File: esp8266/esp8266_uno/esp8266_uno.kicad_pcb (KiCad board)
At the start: 2 copper layers, 68.5 x 53.5 mm, 126 parts, among them J1 Barrel_Jack, P1 USB, Q1 2N2222, Q2 2N2222, SW1 RESET, U1 ESP-12, U2 AMS1117-3.3, U3 CH340G, U4 ESP-13-WROOM-02, X1 12MHz

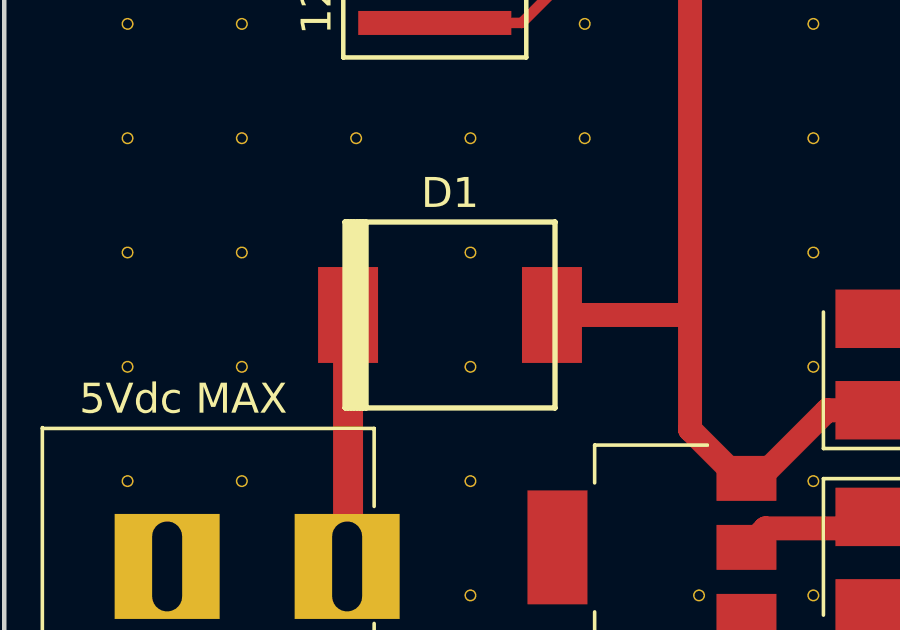
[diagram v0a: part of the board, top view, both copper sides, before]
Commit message: esp8266 uno - fixed input diode orientation
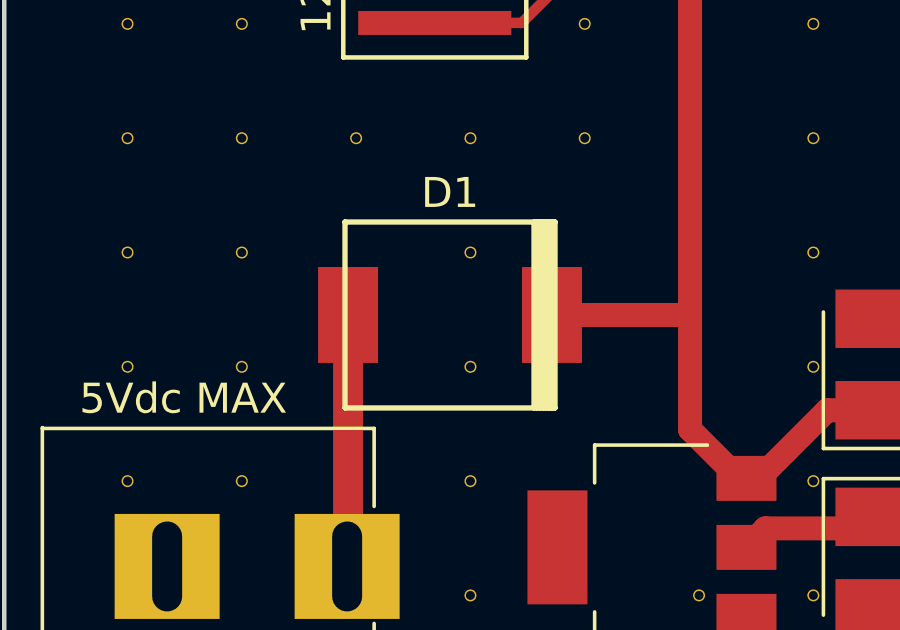
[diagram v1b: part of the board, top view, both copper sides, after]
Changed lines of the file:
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@@
     (add_net "Net-(U3-Pad8)")
+  )
+  (module w_smd_diode:do214ab (layer F.Cu)
+    (at 125.984 116.967 180)
+    (descr DO214AB)
+    (fp_text reference D1 (at 0 4.064 180) (layer F.SilkS)
+      (effects (font (size 1 1) (thickness 0.15)))
+    )
+    (fp_text value SS34 (at 0 2.49936 180) (layer F.SilkS) hide
+      (effects (font (size 0.50038 0.50038) (thickness 0.11938)))
+    )
+    (fp_line (start -3.4 -3.1) (end -3.4 3.0976) (layer F.SilkS) (width 0.1778))
+    (fp_line (start -2.80054 3.0988) (end -2.80054 -3.0988) (layer F.SilkS) (width 0.1778))
+    (fp_line (start -2.8996 -3.0988) (end -2.8996 3.0988) (layer F.SilkS) (width 0.1778))
+    (fp_line (start -3.0012 3.0988) (end -3.0012 -3.0988) (layer F.SilkS) (width 0.1778))
+    (fp_line (start -3.10026 -3.0988) (end -3.10026 3.0988) (layer F.SilkS) (width 0.1778))
+    (fp_line (start -3.19932 3.0988) (end -3.19932 -3.0988) (layer F.SilkS) (width 0.1778))
+    (fp_line (start -3.30092 -3.0988) (end -3.30092 3.0988) (layer F.SilkS) (width 0.1778))
+    (fp_line (start -3.49758 -3.0988) (end 3.49758 -3.0988) (layer F.SilkS) (width 0.1778))
+    (fp_line (start 3.50012 -3.0988) (end 3.50012 3.0988) (layer F.SilkS) (width 0.1778))
+    (fp_line (start 3.50012 3.0988) (end -3.50012 3.0988) (layer F.SilkS) (width 0.1778))
+    (fp_line (start -3.50012 3.0988) (end -3.50012 -3.0988) (layer F.SilkS) (width 0.1778))
+    (pad 2 smd rect (at 3.39852 0 180) (size 1.99898 3.19786) (layers F.Cu F.Paste F.Mask)
+      (net 30 "Net-(D1-Pad2)"))
+    (pad 1 smd rect (at -3.39852 0 180) (size 1.99898 3.19786) (layers F.Cu F.Paste F.Mask)
+      (net 10 +5V))
+    (model ${KISYS3DMOD}/DO_Packages_SMD.3dshapes/DO-214AB.stp
+      (at (xyz 0.1279527559055118 0 0))
+      (scale (xyz 1 1 1))
+      (rotate (xyz 0 0 180))
+    )
   )
   (module myfootprints:ESP-13-WROOM-02 (layer B.Cu)
@@
     )
   )
-  (module w_smd_diode:do214ab (layer F.Cu)
-    (at 125.984 116.967 180)
-    (descr DO214AB)
-    (fp_text reference D1 (at 0 4.064 180) (layer F.SilkS)
-      (effects (font (size 1 1) (thickness 0.15)))
-    )
-    (fp_text value SS34 (at 0 2.49936 180) (layer F.SilkS) hide
-      (effects (font (size 0.50038 0.50038) (thickness 0.11938)))
-    )
-    (fp_line (start 3.40106 -3.0988) (end 3.40106 3.0988) (layer F.SilkS) (width 0.1778))
-    (fp_line (start 3.29946 3.0988) (end 3.29946 -3.0988) (layer F.SilkS) (width 0.1778))
-    (fp_line (start 3.2004 -3.0988) (end 3.2004 3.0988) (layer F.SilkS) (width 0.1778))
-    (fp_line (start 3.0988 3.0988) (end 3.0988 -3.0988) (layer F.SilkS) (width 0.1778))
-    (fp_line (start 2.99974 -3.0988) (end 2.99974 3.0988) (layer F.SilkS) (width 0.1778))
-    (fp_line (start 2.90068 3.0988) (end 2.90068 -3.0988) (layer F.SilkS) (width 0.1778))
-    (fp_line (start 2.79908 -3.0988) (end 2.79908 3.0988) (layer F.SilkS) (width 0.1778))
-    (fp_line (start -3.49758 -3.0988) (end 3.49758 -3.0988) (layer F.SilkS) (width 0.1778))
-    (fp_line (start 3.50012 -3.0988) (end 3.50012 3.0988) (layer F.SilkS) (width 0.1778))
-    (fp_line (start 3.50012 3.0988) (end -3.50012 3.0988) (layer F.SilkS) (width 0.1778))
-    (fp_line (start -3.50012 3.0988) (end -3.50012 -3.0988) (layer F.SilkS) (width 0.1778))
-    (pad 2 smd rect (at 3.39852 0 180) (size 1.99898 3.19786) (layers F.Cu F.Paste F.Mask)
-      (net 30 "Net-(D1-Pad2)"))
-    (pad 1 smd rect (at -3.39852 0 180) (size 1.99898 3.19786) (layers F.Cu F.Paste F.Mask)
-      (net 10 +5V))
-    (model ${KISYS3DMOD}/DO_Packages_SMD.3dshapes/DO-214AB.stp
-      (at (xyz -0.1279527559055118 0 0))
-      (scale (xyz 1 1 1))
-      (rotate (xyz 0 0 0))
-    )
-  )
